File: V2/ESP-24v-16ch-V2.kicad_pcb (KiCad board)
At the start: 2 copper layers, 138 x 67.8 mm, 262 parts, among them J1 VIN, J2 USB, J3 Conn_01x08, J4 Conn_01x08, J5 Conn_01x08, J6 Conn_01x08, J7 ETHERNET, Q1 WPM2015-3/TR, Q10 MMBT2222A/SOT-23-3, Q11 MMBT2222A/SOT-23-3, Q12 MMBT2222A/SOT-23-3, Q13 MMBT2222A/SOT-23-3, Q14 MMBT2222A/SOT-23-3, Q15 MMBT2222A/SOT-23-3, Q16 MMBT2222A/SOT-23-3, Q17 MMBT2222A/SOT-23-3, Q18 MMBT2222A/SOT-23-3, Q19 MMBT2222A/SOT-23-3, Q2 LMUN2211LT1G, Q3 UMH3N, Q4 MMBT2222A/SOT-23-3, Q5 MMBT2222A/SOT-23-3, Q6 MMBT2222A/SOT-23-3, Q7 MMBT2222A/SOT-23-3, Q8 MMBT2222A/SOT-23-3, Q9 MMBT2222A/SOT-23-3, SW1 RESET, U1 SY8089A1AAC, U10 OR-3H4-4, U11 OR-3H4-4, U2 TX4138, U3 CH340C, U4 ESP32-WROOM-32UE-N16, U5 LAN8710A, U6 MCP23017_SS, U7 MCP23017_SS, U8 OR-3H4-4, U9 OR-3H4-4

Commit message: Updates for fabrication
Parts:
- added R129: 2k2/62,5mW/0402, Tales:R_0402_1005Metric, F.Cu at (113.8, 81.9)
- added R130: 2k2/62,5mW/0402, Tales:R_0402_1005Metric, F.Cu at (113.8, 83.2)
- moved R12 3.68 mm to (116.8, 87.6), turned to 0 degrees
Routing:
- net /MCU/I2C_SCL: track 114.9 -> 108.8 mm
- net +3.3V: track 261.2 -> 267.0 mm
- net /GPIO Expanders/MCP1-INTB: track 23.0 -> 26.0 mm
- net +24V: track 260.0 -> 257.4 mm
- net /GPIO Expanders/IN13: track 30.7 -> 32.7 mm
- net Net-(Q3A-C1): track 49.2 -> 47.3 mm
- net /GPIO Expanders/MCP1-INTA: track 27.2 -> 29.0 mm, vias 2 -> 3
- net GND: track 550.4 -> 548.7 mm
- net /MCU/I2C_SDA: track 114.7 -> 113.1 mm
- net /LAN/EMAC_TXD1: track 37.4 -> 35.9 mm
- net Net-(U3-RXD): track 44.0 -> 45.3 mm
- net Net-(U3-TXD): track 41.5 -> 42.8 mm
- net Net-(D35-A): track 65.4 -> 66.4 mm
- net /MCU/PHY_PWR: track 31.5 -> 32.3 mm
- net /GPIO Expanders/IN9: track 50.5 -> 49.7 mm

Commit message: Final tweaks
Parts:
- moved C14 4.28 mm to (140.6, 112.0), turned to 90 degrees
- moved D1 1.78 mm to (95.2, 122.3)
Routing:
- net Net-(C14-Pad1): track 25.2 -> 20.8 mm
- net Net-(D27-A): track 69.0 -> 67.1 mm
- net Net-(D28-A): track 72.8 -> 71.1 mm
- net Net-(D29-A): track 75.9 -> 74.2 mm
- net Net-(D30-A): track 78.9 -> 77.4 mm
- net +24V: track 257.4 -> 256.7 mm
- net /Power/VIN: track 4.44 -> 5.18 mm

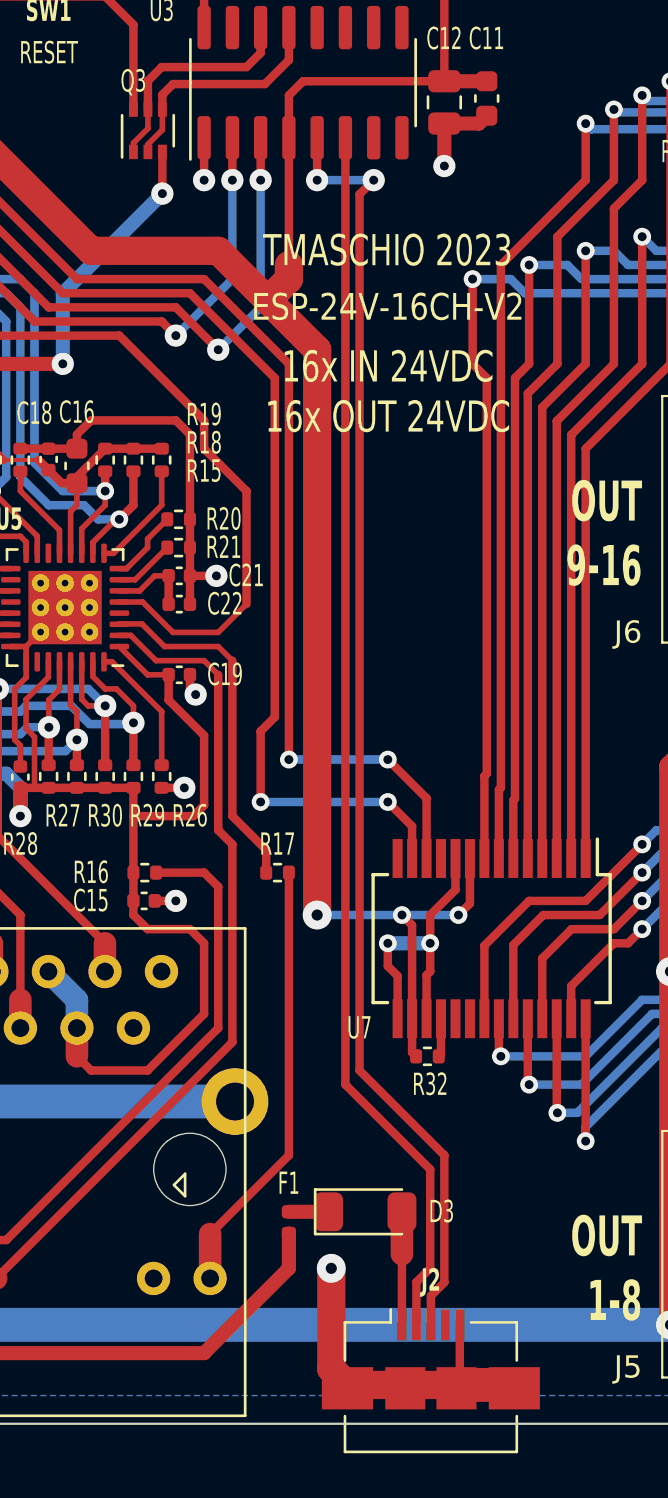
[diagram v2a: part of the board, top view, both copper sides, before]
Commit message: Adjustments for fabrication.
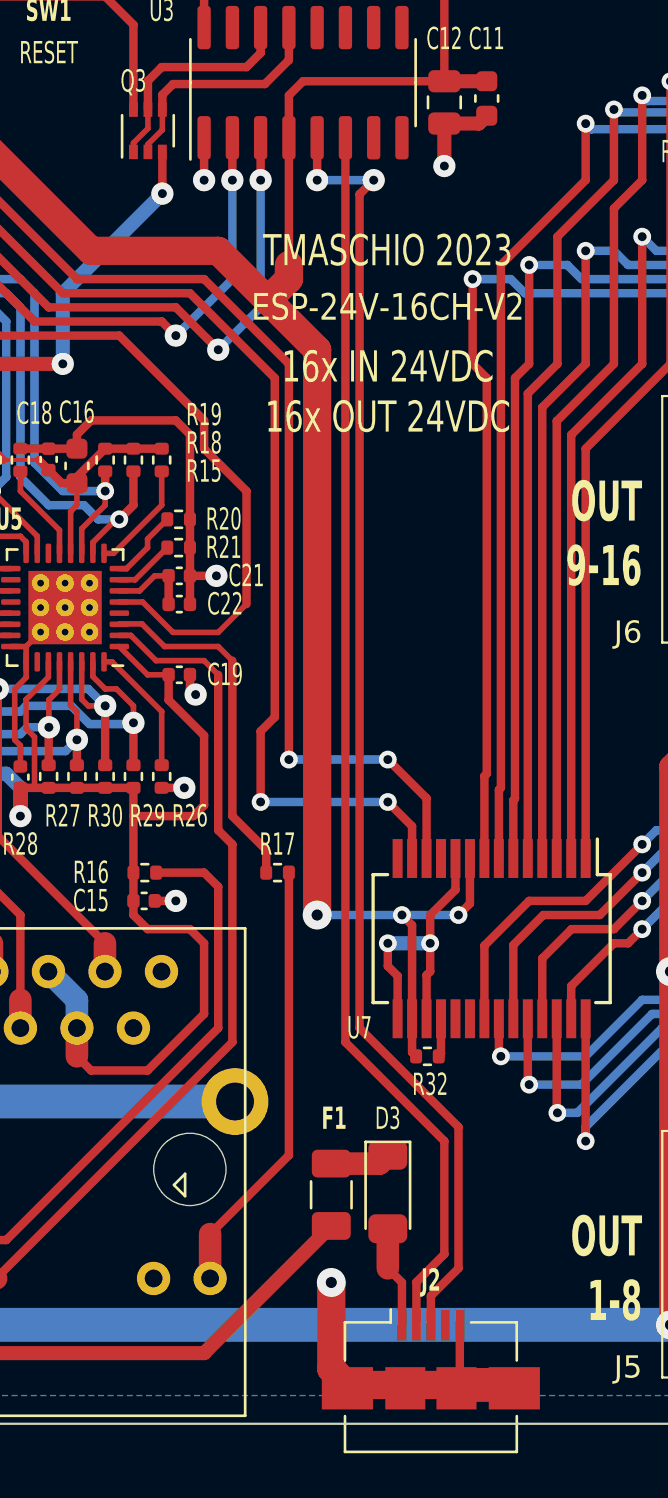
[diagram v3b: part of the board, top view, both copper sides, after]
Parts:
- F1: footprint Tales:Fuse_0402_1005Metric -> Fuse:Fuse_1206_3216Metric
- moved F1 2.28 mm to (163.2, 121.8)
- moved D3 1.35 mm to (165.7, 121.7), turned to -90 degrees
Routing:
- net +5V: track 105.8 -> 106.9 mm
- net Net-(D3-K): track 1.78 -> 2.70 mm
- net GND: track 549.1 -> 548.5 mm
- net /MCU/USB_D-: track 55.0 -> 55.6 mm
- net /MCU/USB_D+: track 57.8 -> 58.3 mm

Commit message: Update ESP-24v-16ch-V2.kicad_pcb
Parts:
- moved C11 0.64 mm to (170.2, 71.9)
- moved C12 0.64 mm to (168.3, 72.1)
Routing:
- net Net-(U3-TXD): track 42.8 -> 36.7 mm
- net Net-(U3-RXD): track 45.3 -> 39.7 mm
- net /MCU/USB_D+: track 58.3 -> 60.5 mm, vias 2 -> 0
- net /MCU/I2C_SCL: track 108.8 -> 111.0 mm
- net /LAN/EMAC_RXD0: track 49.9 -> 50.9 mm
- net /MCU/I2C_SDA: track 113.1 -> 113.9 mm
- net /LAN/EMAC_RXD1: track 50.9 -> 51.5 mm
- net GND: track 548.5 -> 548.8 mm, vias 108 -> 107

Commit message: Improvements to the PCB layout
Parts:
- moved U7 11.4 mm to (170.4, 98.8)
- moved R32 11.4 mm to (167.5, 104.1)
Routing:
- net /MCU/I2C_SDA: track 113.9 -> 101.2 mm
- net +3.3V: track 266.6 -> 255.1 mm
- net /GPIO Expanders/OUT16: track 60.5 -> 48.9 mm
- net /GPIO Expanders/OUT10: track 39.8 -> 28.4 mm
- net /GPIO Expanders/OUT14: track 53.2 -> 41.8 mm
- net /GPIO Expanders/OUT12: track 46.5 -> 35.0 mm
- net /MCU/I2C_SCL: track 111.0 -> 99.6 mm
- net /GPIO Expanders/OUT11: track 47.8 -> 36.9 mm
- net /GPIO Expanders/OUT9: track 42.9 -> 32.0 mm
- net /GPIO Expanders/OUT13: track 53.7 -> 43.2 mm
- net /GPIO Expanders/OUT15: track 59.8 -> 49.6 mm
- net /GPIO Expanders/OUT2: track 19.6 -> 26.4 mm
- net /GPIO Expanders/OUT4: track 25.2 -> 31.4 mm
- net /GPIO Expanders/OUT6: track 30.8 -> 36.5 mm
- net /GPIO Expanders/OUT8: track 36.7 -> 41.5 mm
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
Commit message: Improvements to PCB design
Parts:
- moved R17 11.7 mm to (156.3, 96.5)
- moved C19 0.63 mm to (156.4, 97.8)
- moved F1 0.38 mm to (163.2, 121.4)
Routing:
- net GND: track 545.6 -> 516.2 mm, vias 107 -> 110
- net +3.3V: track 255.1 -> 235.7 mm
- net /LAN/LED_Y_A: track 15.9 -> 2.31 mm
- net Net-(J7-Pad12): track 19.7 -> 33.1 mm
- net Net-(U3-RXD): track 39.7 -> 29.0 mm, vias 4 -> 2
- net Net-(U3-TXD): track 36.7 -> 27.7 mm, vias 4 -> 2
- net /MCU/I2C_SDA: track 101.2 -> 108.4 mm, vias 6 -> 4
- net +3.3VLAN: track 38.5 -> 44.7 mm, vias 2 -> 3
- net /MCU/I2C_SCL: track 99.6 -> 105.6 mm, vias 6 -> 4
- net /LAN/EMAC_RX: track 45.1 -> 39.7 mm
- net /LAN/EMAC_TXD1: track 36.3 -> 40.4 mm
- net +3.3VA: track 70.2 -> 72.8 mm
- net Net-(Q3B-C2): track 28.8 -> 30.7 mm, vias 4 -> 2
- net /LAN/EMAC_RXD1: track 51.5 -> 49.8 mm, vias 2 -> 4
- net /LAN/EMAC_RXD0: track 50.9 -> 49.5 mm, vias 2 -> 4
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
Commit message: Improvements to the PCB design
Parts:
- moved F1 1.42 mm to (164.5, 120.8)
- moved D3 1.42 mm to (167.0, 121.0)
- moved R24 1.27 mm to (141.1, 93.3)
- moved C17 1.27 mm to (140.8, 94.6)
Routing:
- net +5V: track 107.3 -> 93.8 mm, vias 2 -> 4
- net /LAN/EMAC_RXD0: track 49.5 -> 45.4 mm, vias 4 -> 2
- net /MCU/I2C_SDA: track 108.4 -> 104.4 mm
- net /LAN/EMAC_RXD1: track 49.8 -> 46.5 mm, vias 4 -> 2
- net +3.3VLAN: track 44.7 -> 42.0 mm, vias 3 -> 2
- net /MCU/I2C_SCL: track 105.6 -> 103.0 mm
- net /LAN/EMAC_MDIO: track 29.8 -> 32.0 mm
- net GND: track 516.2 -> 515.2 mm
- net /GPIO Expanders/OUT9: track 32.0 -> 31.1 mm
- net /LAN/RD-: track 32.9 -> 32.0 mm
- net +3.3VA: track 72.8 -> 72.0 mm
- net /Power/USB_VBUS: track 4.58 -> 5.22 mm
- net /GPIO Expanders/IN15: track 42.4 -> 41.8 mm
- net /GPIO Expanders/OUT11: track 36.9 -> 36.3 mm
- net Net-(U5-~{RST}): track 9.00 -> 8.48 mm
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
